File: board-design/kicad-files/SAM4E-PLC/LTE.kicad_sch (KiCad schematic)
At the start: 61 parts, among them J1 SIM_Card_Shielded, Q1 BC817, Q2 BC817, U3 EC21, U4 TXS0108EPW, U5 TXS0108EPW

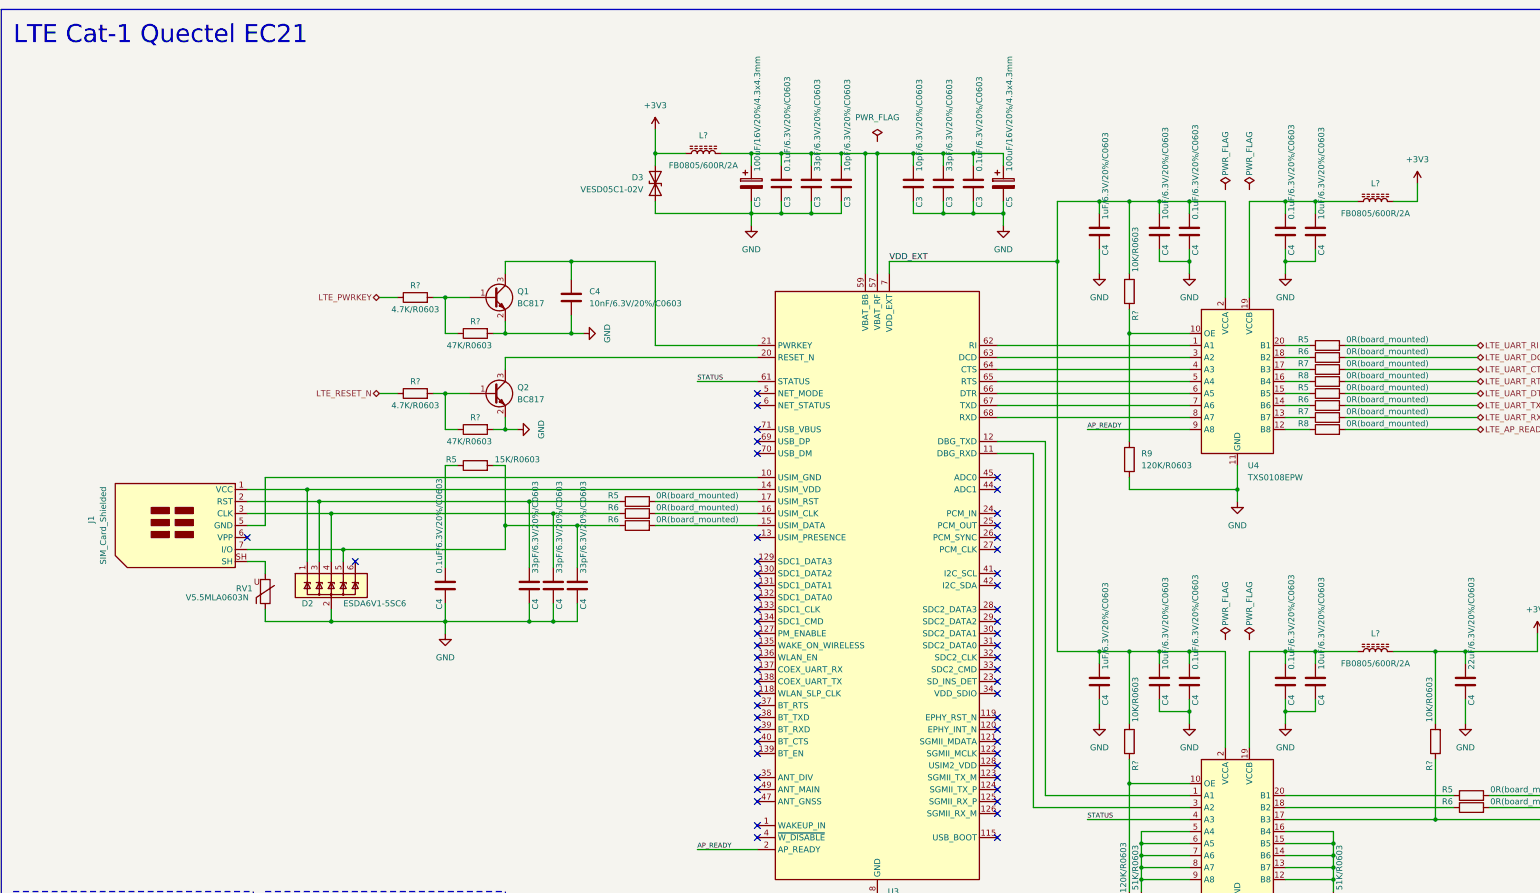
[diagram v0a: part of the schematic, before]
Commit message: [UPDATE]
Refactored schematic for LTE, Power and other schematic sub-sheets.

Signed-off-by: Nicolae-Andrei Vasile <vasilenicolaeandrei@gmail.com>
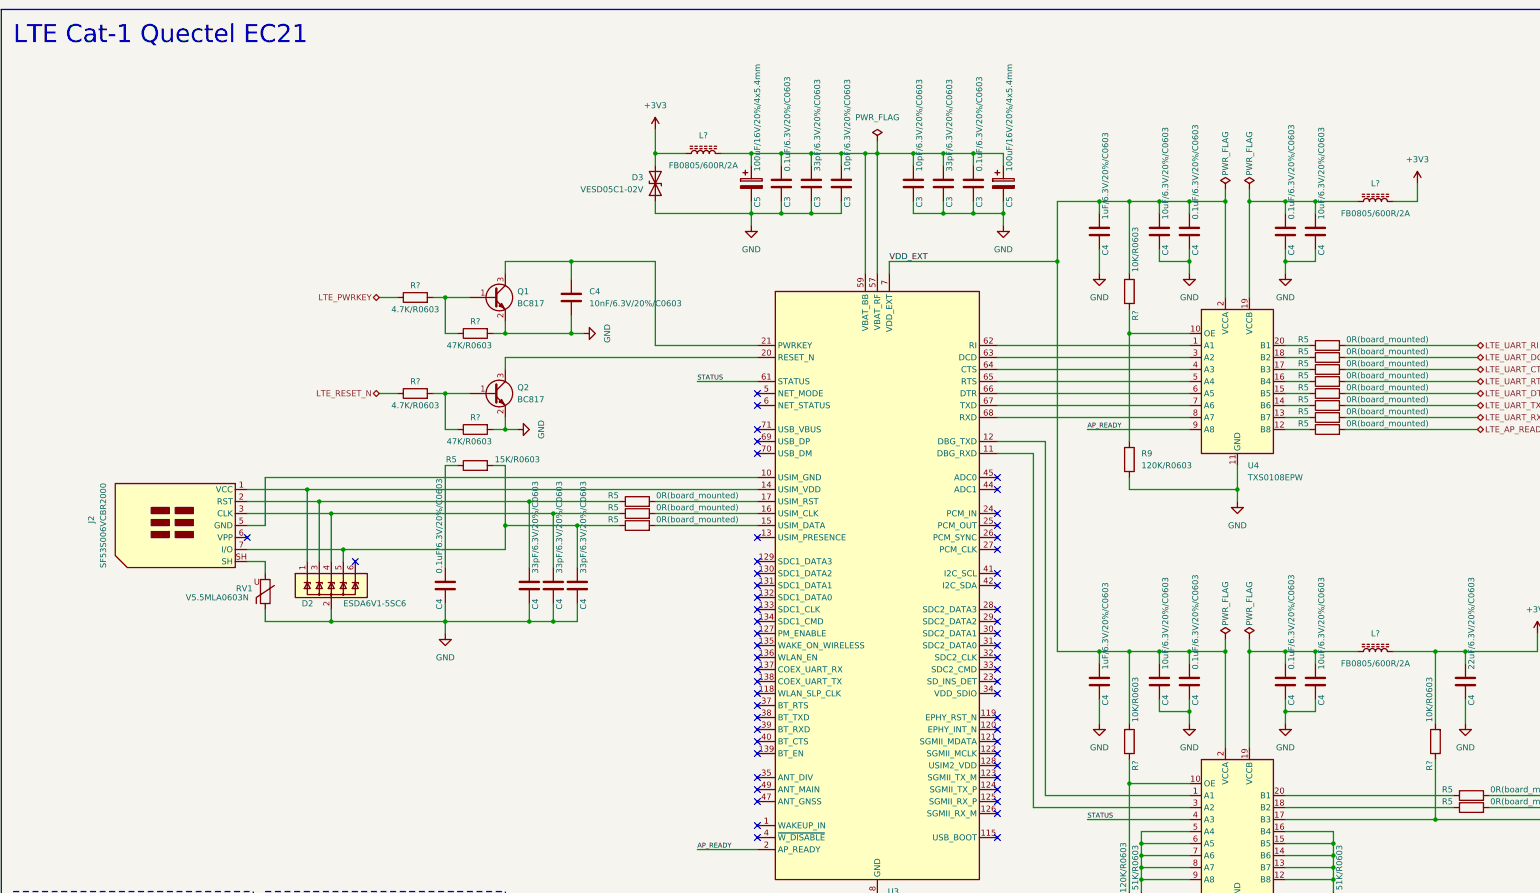
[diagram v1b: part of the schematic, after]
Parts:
- removed L? (x3): FB0805/600R/2A, symbol Device:L_Ferrite
- removed R5 (x3), R6 (x5), R7 (x2), R8 (x2): 0R(board_mounted), symbol Device:R
- added L? (x3): FB0805/600R/2A, Inductor_SMD:L_0805_2012Metric, symbol Device:L_Ferrite
- added R5 (x12): 0R(board_mounted), Resistor_SMD:R_0402_1005Metric, symbol Device:R
- C3, C4: footprint (none) -> Capacitor_SMD:C_0603_1608Metric
- C5: value 100uF/16V/20%/4.3x4.3mm -> 100uF/16V/20%/4x5.4mm; footprint (none) -> Capacitor_SMD:CP_Elec_4x5.4
- J2: renamed from J1; value SIM_Card_Shielded -> SF53S006VCBR2000; footprint (none) -> Connector_Card:microSIM_JAE_SF53S006VCBR2000
- R5, R9, RV1: footprint (none) -> Resistor_SMD:R_0603_1608Metric
- R5: footprint (none) -> Resistor_SMD:R_0402_1005Metric
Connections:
- net +3V3: now also L?.1, L?.2, L?.2
- net LTE_AP_READY: now also R5.2
- net LTE_UART_CTS: now also R5.2
- net LTE_UART_DBG_RXD: now also R5.2
- net LTE_UART_DBG_TXD: now also R5.2
- net LTE_UART_DCD: now also R5.2
- net LTE_UART_DTR: now also R5.2
- net LTE_UART_RI: now also R5.2
- net LTE_UART_RTS: now also R5.2
- net LTE_UART_RXD: now also R5.2
- net LTE_UART_TXD: now also R5.2
- net at U4.18 (B2): now also R5.1
- net at C4.1, D2.5 (IO4), J2.7 (I/O)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: now also R5.1
- net at U5.18 (B2): now also R5.1
- net at U4.15 (B5): now also R5.1
- net at C4.1, D2.4 (IO3), J2.3 (CLK): now also R5.1
- net at C3.1, C3.1, C3.1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: now also L?.2
- net at U5.20 (B1): now also R5.1
- net at C4.1, C4.1, U4.19 (VCCB): now also L?.1
- net at U3.16 (USIM_CLK): now also R5.2
- net at U4.16 (B4): now also R5.1
- net at C4.1, C4.1, U5.19 (VCCB): now also L?.1
- net at U4.12 (B8): now also R5.1
- net at U4.13 (B7): now also R5.1
- net at U4.14 (B6): now also R5.1
- net at U4.17 (B3): now also R5.1
- net at U4.20 (B1): now also R5.1
- net at U3.15 (USIM_DATA): now also R5.2

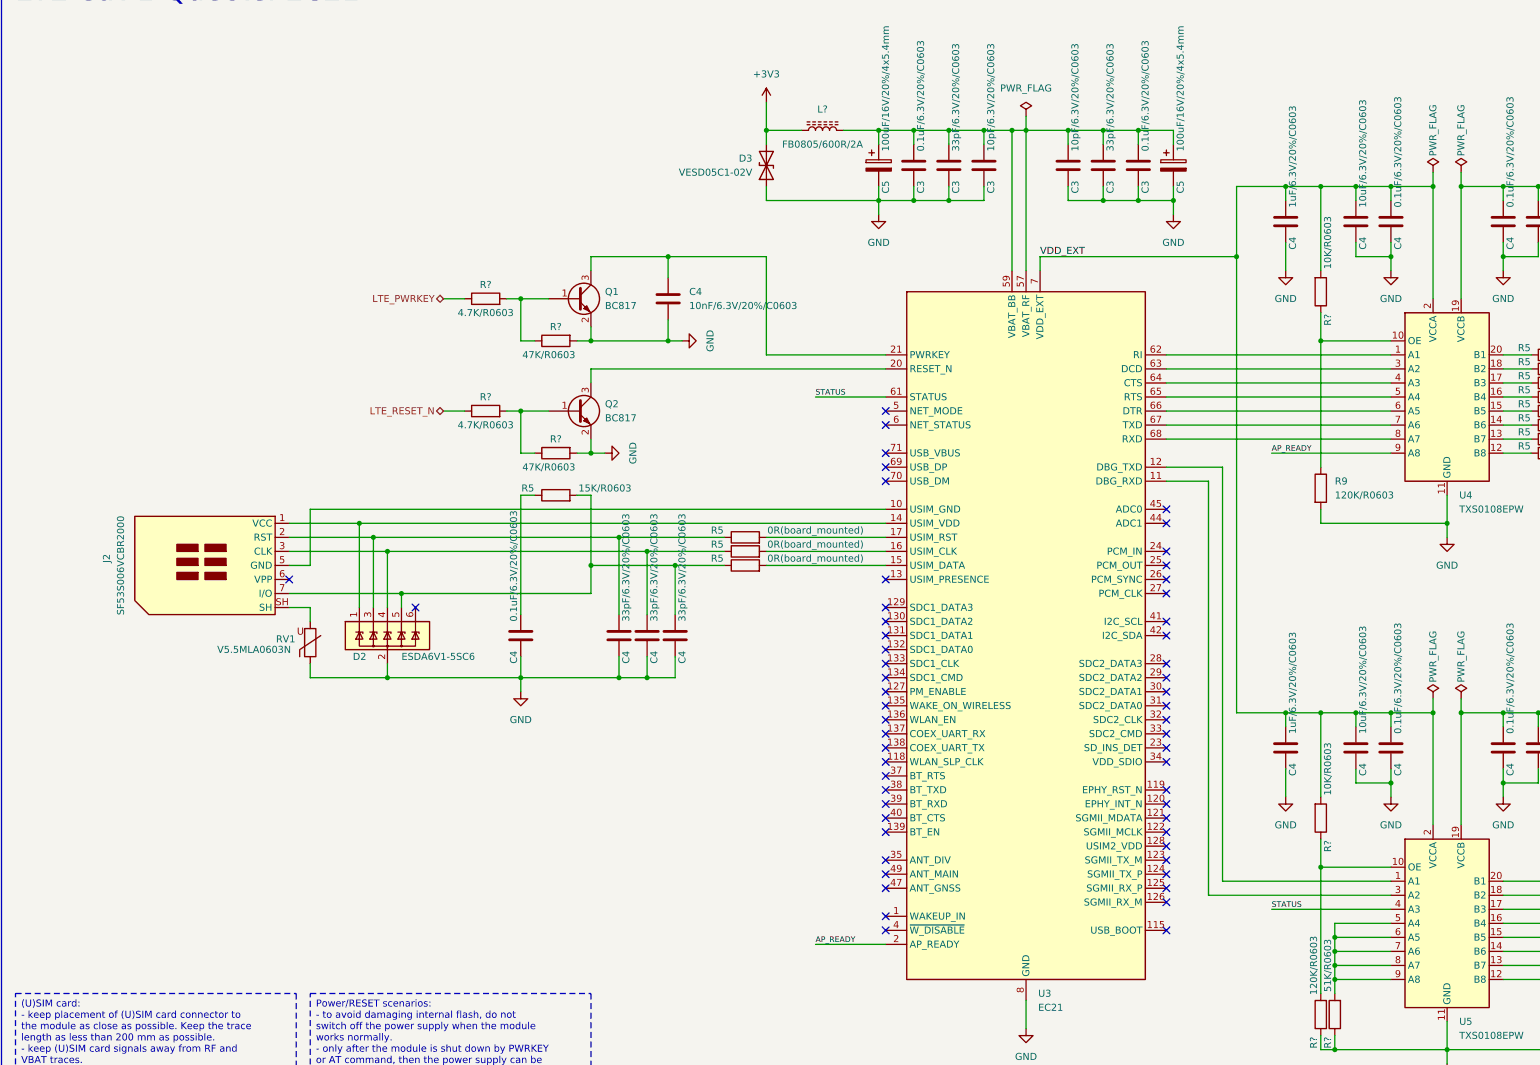
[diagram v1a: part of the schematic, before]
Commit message: [UPDATE]
First draft of SAM4E-PLC schematic completed.

Signed-off-by: Nicolae-Andrei Vasile <vasilenicolaeandrei@gmail.com>
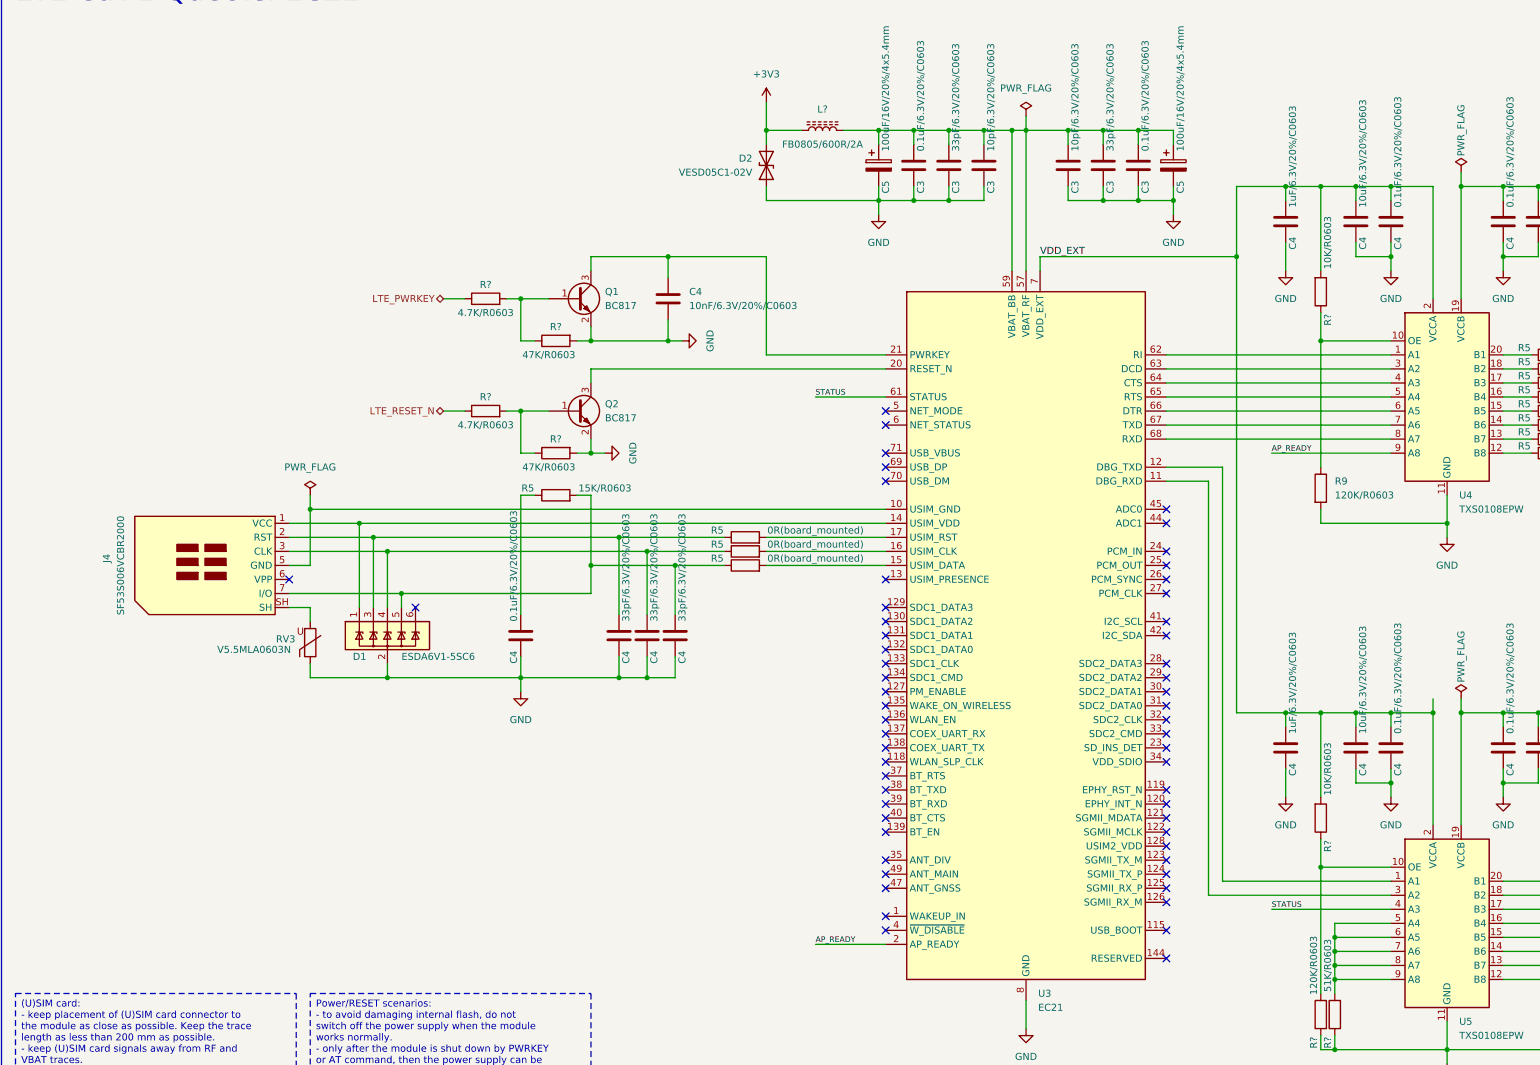
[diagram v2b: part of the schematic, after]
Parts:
- renumbered D2 to D1, D3 to D2, J2 to J4, RV1 to RV3
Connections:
- no-connect marks 56 -> 57

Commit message: [UPDATE]
Work in progress.

Signed-off-by: Nicolae-Andrei Vasile <vasilenicolaeandrei@gmail.com>
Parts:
- renumbered D1 to D2, D2 to D3
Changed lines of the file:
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@@
   (symbol (lib_id "Power_Protection:ESDA6V1-5SC6") (at 87.63 139.7 0) (unit 1)
     (in_bom yes) (on_board yes) (dnp no)
-    (property "Reference" "D1" (at 83.82 143.51 0)
+    (property "Reference" "D2" (at 83.82 143.51 0)
       (effects (font (size 1.27 1.27)) (justify right))
     )
@@
       (project "SAM4E-PLC"
         (path "/93076d8a-73da-4f5d-b7f2-28678f1db77d/62dc9d33-a289-4ad9-a327-b6290b31f4f3"
-          (reference "D1") (unit 1)
+          (reference "D2") (unit 1)
         )
       )
@@
   (symbol (lib_id "SparkFun-DiscreteSemi:D_TVS") (at 156.21 54.61 90) (unit 1)
     (in_bom yes) (on_board yes) (dnp no)
-    (property "Reference" "D2" (at 153.67 53.34 90)
+    (property "Reference" "D3" (at 153.67 53.34 90)
       (effects (font (size 1.27 1.27)) (justify left))
     )
@@
       (project "SAM4E-PLC"
         (path "/93076d8a-73da-4f5d-b7f2-28678f1db77d/62dc9d33-a289-4ad9-a327-b6290b31f4f3"
-          (reference "D2") (unit 1)
+          (reference "D3") (unit 1)
         )
       )

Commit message: [UPDATE]
Work in progress.

Signed-off-by: Nicolae-Andrei Vasile <vasilenicolaeandrei@gmail.com>
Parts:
- renumbered D2 to D3, D3 to D4, J4 to J5
